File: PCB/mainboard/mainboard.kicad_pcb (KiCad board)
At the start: 2 copper layers, 100 x 68 mm, 1 part, among them IC1 STM32H743ZIT6

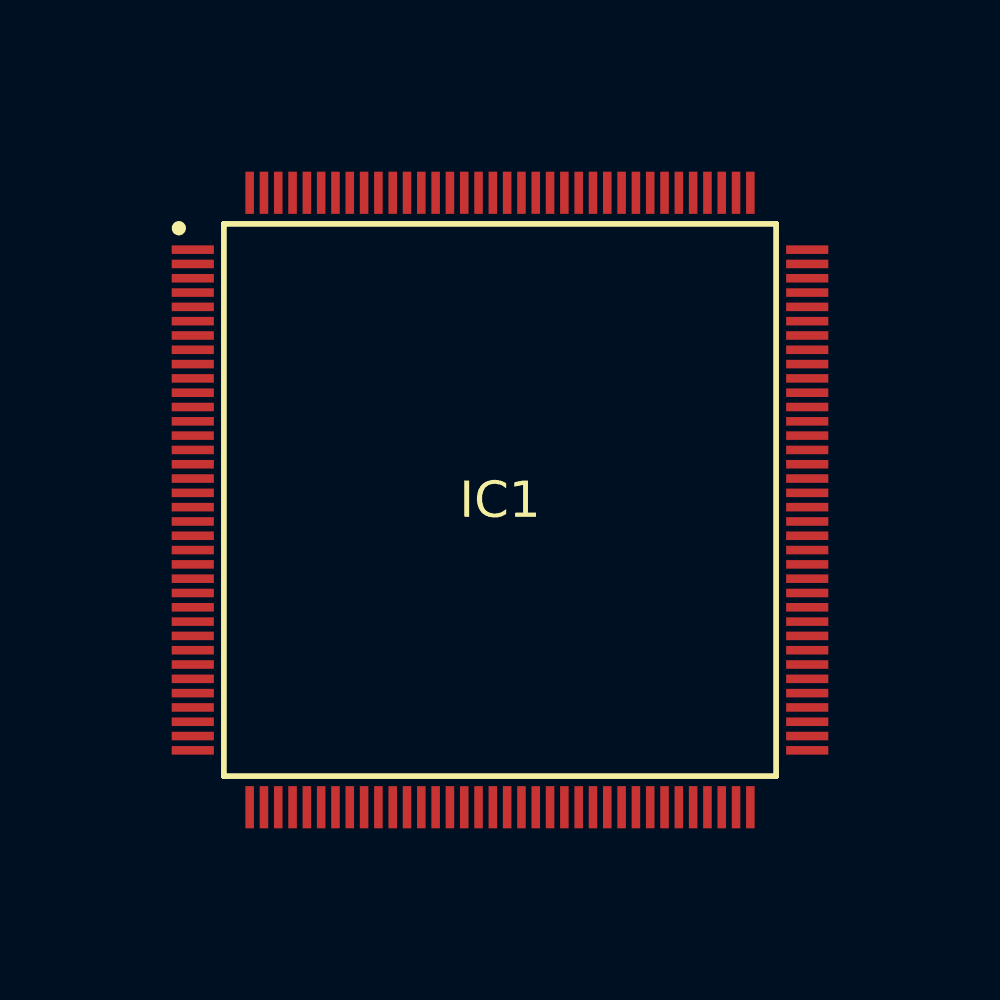
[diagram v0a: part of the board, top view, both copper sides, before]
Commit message: upgrades to STM32 Board
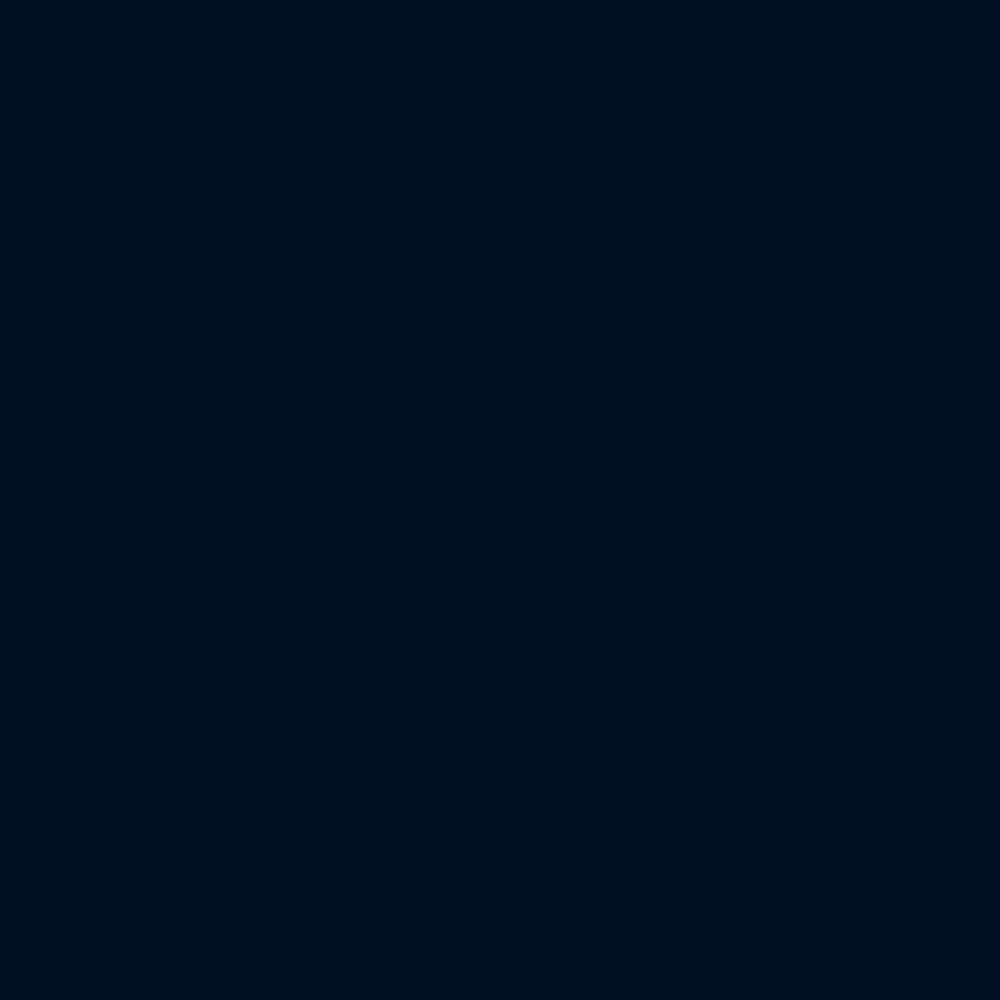
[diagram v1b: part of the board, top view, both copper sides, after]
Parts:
- removed IC1: STM32H743ZIT6, lib:QFP50P2200X2200X160-144N

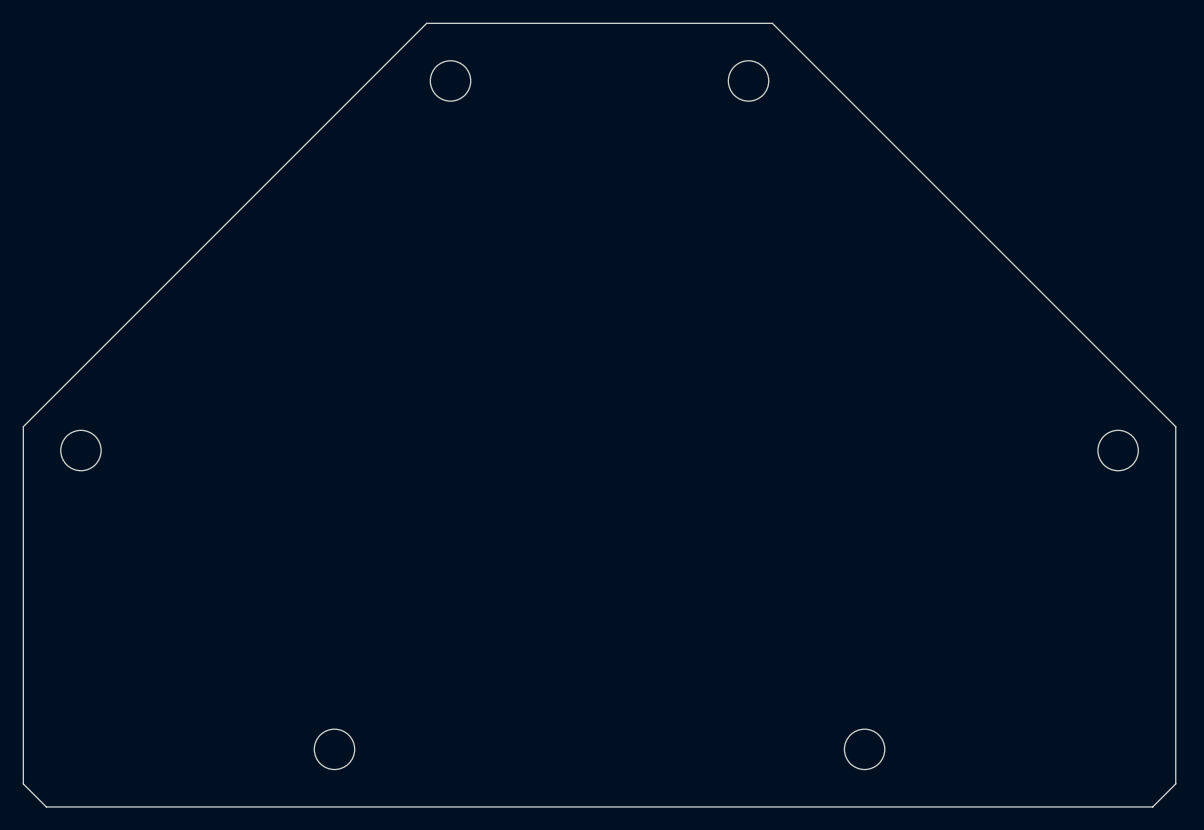
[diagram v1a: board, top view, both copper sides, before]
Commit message: Made the Mainboard BCP Part Layout
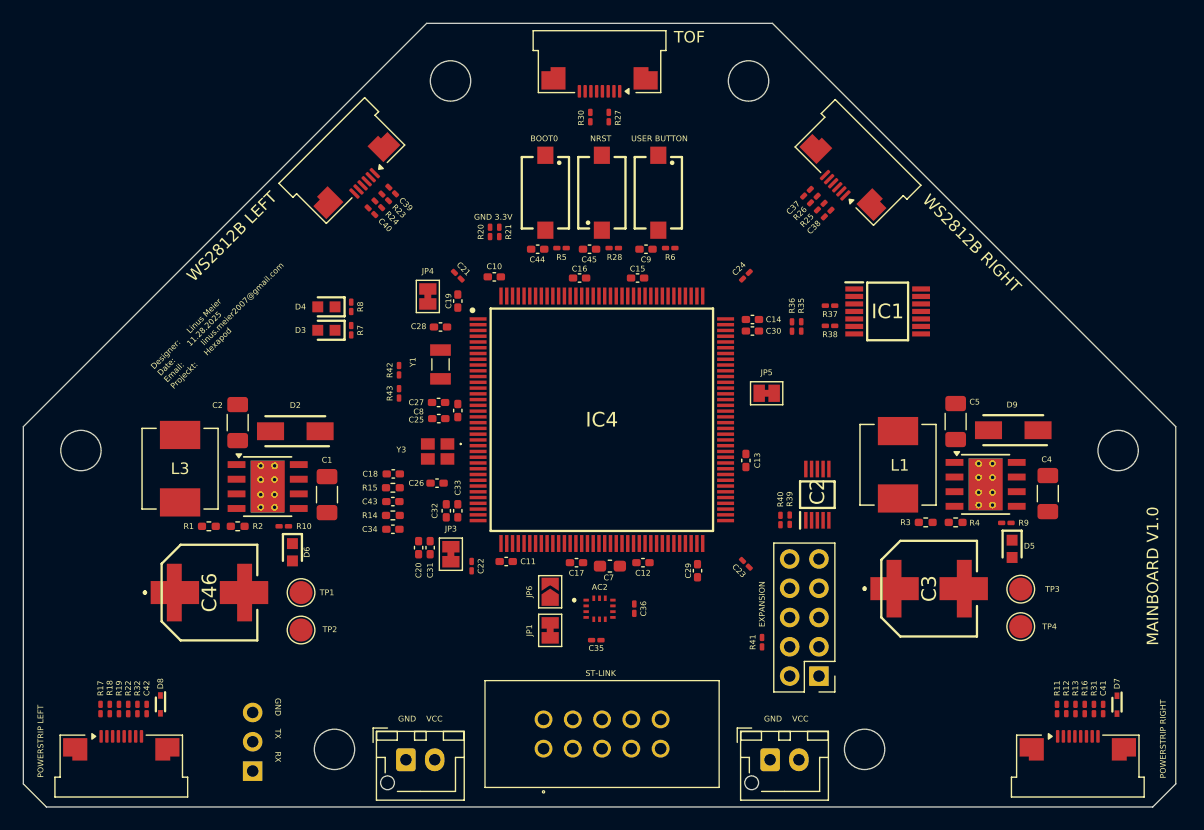
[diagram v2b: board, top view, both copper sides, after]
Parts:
- added AC2: LSM6DSOTR, lib:LSM6DS3USTR, F.Cu at (149.5, 119.3)
- added BOOT0: 434121025816, lib:434121025816, F.Cu at (144.8, 83.2)
- added C1: 10u, Capacitor_SMD:C_1206_3216Metric_Pad1.33x1.80mm_HandSolder, F.Cu at (125.8, 109.4)
- added C10: 100nF, Capacitor_SMD:C_0402_1005Metric_Pad0.74x0.62mm_HandSolder, F.Cu at (140.4, 90.5)
- added C11: 100nF, Capacitor_SMD:C_0402_1005Metric_Pad0.74x0.62mm_HandSolder, F.Cu at (141.4, 115.2)
- added C12: 100nF, Capacitor_SMD:C_0402_1005Metric_Pad0.74x0.62mm_HandSolder, F.Cu at (153.3, 115.3)
- added C13: 100nF, Capacitor_SMD:C_0402_1005Metric_Pad0.74x0.62mm_HandSolder, F.Cu at (162.2, 106.4)
- added C14: 100nF, Capacitor_SMD:C_0402_1005Metric_Pad0.74x0.62mm_HandSolder, F.Cu at (162.8, 94.2)
- added C15: 100nF, Capacitor_SMD:C_0402_1005Metric_Pad0.74x0.62mm_HandSolder, F.Cu at (152.8, 90.6)
- added C16: 100nF, Capacitor_SMD:C_0402_1005Metric_Pad0.74x0.62mm_HandSolder, F.Cu at (147.8, 90.6)
- added C17: 100nF, Capacitor_SMD:C_0402_1005Metric_Pad0.74x0.62mm_HandSolder, F.Cu at (147.5, 115.3)
- added C18: 100nF, Capacitor_SMD:C_0402_1005Metric_Pad0.74x0.62mm_HandSolder, F.Cu at (131.6, 107.6)
- added C19: 1uF, Capacitor_SMD:C_0402_1005Metric_Pad0.74x0.62mm_HandSolder, F.Cu at (137.2, 92.6)
- added C2: 10n, Capacitor_SMD:C_1206_3216Metric_Pad1.33x1.80mm_HandSolder, F.Cu at (118.1, 103.1)
- added C20: 1uF, Capacitor_SMD:C_0402_1005Metric_Pad0.74x0.62mm_HandSolder, F.Cu at (133.8, 114.0)
- added C21: 1u, Capacitor_SMD:C_0201_0603Metric_Pad0.64x0.40mm_HandSolder, F.Cu at (137.2, 90.4)
- added C22: 1u, Capacitor_SMD:C_0201_0603Metric_Pad0.64x0.40mm_HandSolder, F.Cu at (138.4, 115.6)
- added C23: 1u, Capacitor_SMD:C_0201_0603Metric_Pad0.64x0.40mm_HandSolder, F.Cu at (162.2, 115.4)
- added C24: 1u, Capacitor_SMD:C_0201_0603Metric_Pad0.64x0.40mm_HandSolder, F.Cu at (162.2, 90.4)
- added C25: 10pF, Capacitor_SMD:C_0402_1005Metric_Pad0.74x0.62mm_HandSolder, F.Cu at (135.6, 102.8)
- added C26: 10pF, Capacitor_SMD:C_0402_1005Metric_Pad0.74x0.62mm_HandSolder, F.Cu at (135.4, 108.4)
- added C27: 8pF, Capacitor_SMD:C_0402_1005Metric_Pad0.74x0.62mm_HandSolder, F.Cu at (135.5, 101.4)
- added C28: 8pF, Capacitor_SMD:C_0402_1005Metric_Pad0.74x0.62mm_HandSolder, F.Cu at (135.7, 94.8)
- added C29: 2.2u, Capacitor_SMD:C_0402_1005Metric_Pad0.74x0.62mm_HandSolder, F.Cu at (158.0, 116.0)
- added C3: EEE-FP0J331AV 220u, lib:EEEFP0J331AV, F.Cu at (178.1, 117.6)
- added C30: 2.2u, Capacitor_SMD:C_0402_1005Metric_Pad0.74x0.62mm_HandSolder, F.Cu at (162.8, 95.2)
- added C31: 100nF, Capacitor_SMD:C_0402_1005Metric_Pad0.74x0.62mm_HandSolder, F.Cu at (134.8, 114.0)
- added C32: 1uF, Capacitor_SMD:C_0402_1005Metric_Pad0.74x0.62mm_HandSolder, F.Cu at (136.2, 110.8)
- added C33: 100nF, Capacitor_SMD:C_0402_1005Metric_Pad0.74x0.62mm_HandSolder, F.Cu at (137.2, 110.8)
- added C34: 100nF, Capacitor_SMD:C_0402_1005Metric_Pad0.74x0.62mm_HandSolder, F.Cu at (131.6, 112.4)
- added C35: 100n, Capacitor_SMD:C_0201_0603Metric_Pad0.64x0.40mm_HandSolder, F.Cu at (149.2, 122.0)
- added C36: 100n, Capacitor_SMD:C_0201_0603Metric_Pad0.64x0.40mm_HandSolder, F.Cu at (152.5, 119.3)
- added C37: 1u, Capacitor_SMD:C_0201_0603Metric_Pad0.64x0.40mm_HandSolder, F.Cu at (167.5, 83.2)
- added C38: 1u, Capacitor_SMD:C_0201_0603Metric_Pad0.64x0.40mm_HandSolder, F.Cu at (169.3, 85.0)
- added C39: 1u, Capacitor_SMD:C_0201_0603Metric_Pad0.64x0.40mm_HandSolder, F.Cu at (131.5, 83.0)
- added C4: 10u, Capacitor_SMD:C_1206_3216Metric_Pad1.33x1.80mm_HandSolder, F.Cu at (188.4, 109.3)
- added C40: 1u, Capacitor_SMD:C_0201_0603Metric_Pad0.64x0.40mm_HandSolder, F.Cu at (129.7, 84.8)
- added C41: 100n, Capacitor_SMD:C_0201_0603Metric_Pad0.64x0.40mm_HandSolder, F.Cu at (193.2, 128.0)
- added C42: 100n, Capacitor_SMD:C_0201_0603Metric_Pad0.64x0.40mm_HandSolder, F.Cu at (110.2, 128.0)
- added C43: 100nF, Capacitor_SMD:C_0402_1005Metric_Pad0.74x0.62mm_HandSolder, F.Cu at (131.6, 110.0)
- added C44: 100n, Capacitor_SMD:C_0402_1005Metric_Pad0.74x0.62mm_HandSolder, F.Cu at (144.1, 88.1)
- added C45: 100n, Capacitor_SMD:C_0402_1005Metric_Pad0.74x0.62mm_HandSolder, F.Cu at (148.6, 88.1)
- added C46: EEE-FP0J331AV 220u, lib:EEEFP0J331AV, F.Cu at (115.7, 117.9)
- added C5: 10n, Capacitor_SMD:C_1206_3216Metric_Pad1.33x1.80mm_HandSolder, F.Cu at (180.4, 103.1)
- added C7: 4.7uF, Capacitor_SMD:C_0603_1608Metric_Pad1.08x0.95mm_HandSolder, F.Cu at (150.4, 115.6)
- added C8: 100nF, Capacitor_SMD:C_0402_1005Metric_Pad0.74x0.62mm_HandSolder, F.Cu at (137.2, 102.1)
- added C9: 100n, Capacitor_SMD:C_0402_1005Metric_Pad0.74x0.62mm_HandSolder, F.Cu at (153.5, 88.1)
- added D2: B340A-13-F, lib:DIOM5226X240N, F.Cu at (123.1, 103.9)
- added D3: LED_Red, lib:LEDC1608X70N, F.Cu at (125.8, 95.1)
- added D4: LED_Geen, lib:LEDC1608X70N, F.Cu at (125.8, 93.1)
- added D5: LED_Geen, lib:LEDC1608X70N, F.Cu at (185.3, 114.1)
- added D6: LED_Geen, lib:LEDC1608X70N, F.Cu at (122.8, 114.4)
- added D7: BZT585B3V3T-7, lib:SODFL1608X65N, F.Cu at (194.4, 127.6)
- added D8: BZT585B3V3T-7, lib:SODFL1608X65N, F.Cu at (111.4, 127.6)
- added D9: B340A-13-F, lib:DIOM5226X240N, F.Cu at (185.4, 103.8)
- added EXPANSION: Conn_02x05_Counter_Clockwise, Connector_PinHeader_2.54mm:PinHeader_2x05_P2.54mm_Vertical, F.Cu at (168.5, 125.1)
- added GND    VCC: Right Strip Power, Connector_JST:JST_XH_B2B-XH-AM_1x02_P2.50mm_Vertical, F.Cu at (164.3, 132.4)
- added GND    VCC: Left Strip Power, Connector_JST:JST_XH_B2B-XH-AM_1x02_P2.50mm_Vertical, F.Cu at (132.7, 132.4)
- added IC1: 74HCT125T14-13, lib:SOP65P640X120-14N, F.Cu at (174.5, 93.5)
- added IC2: SP4065-08ATG, lib:SOP50P488X110-10N, F.Cu at (168.4, 109.4)
- added IC4: STM32H743ZIT6, lib:QFP50P2200X2200X160-144N, F.Cu at (149.7, 102.9)
- added J10: Uart Connector to pi5, Connector_PinSocket_2.54mm:PinSocket_1x03_P2.54mm_Vertical, B.Cu at (119.4, 133.4)
- added JP1: SolderJumper_2_Bridged, Jumper:SolderJumper-2_P1.3mm_Bridged_Pad1.0x1.5mm, F.Cu at (145.2, 121.2)
- added JP3: SolderJumper_2_Bridged, Jumper:SolderJumper-2_P1.3mm_Bridged_Pad1.0x1.5mm, F.Cu at (136.6, 114.6)
- added JP4: SolderJumper_2_Bridged, Jumper:SolderJumper-2_P1.3mm_Bridged_Pad1.0x1.5mm, F.Cu at (134.6, 92.2)
- added JP5: SolderJumper_2_Bridged, Jumper:SolderJumper-2_P1.3mm_Bridged_Pad1.0x1.5mm, F.Cu at (164.0, 100.6)
- added JP6: SolderJumper_2_Open, Jumper:SolderJumper-2_P1.3mm_Open_TrianglePad1.0x1.5mm, F.Cu at (145.2, 117.8)
- added L1: MGAH06033R3M-10, lib:IND_MGAH06033R3M-10, F.Cu at (175.4, 106.8)
- added L3: MGAH06033R3M-10, lib:IND_MGAH06033R3M-10, F.Cu at (113.1, 107.1)
- added NRST: 434121025816, lib:434121025816, F.Cu at (149.7, 83.2)
- added POWERSTRIP LEFT: Left Strip, Connector_FFC-FPC:Amphenol_F32Q-1A7x1-11008_1x08-1MP_P0.5mm_Horizontal, F.Cu at (108.0, 133.3)
- added POWERSTRIP RIGHT: Right Strip, Connector_FFC-FPC:Amphenol_F32Q-1A7x1-11008_1x08-1MP_P0.5mm_Horizontal, F.Cu at (191.0, 133.3)
- added R1: 51k, Resistor_SMD:R_0402_1005Metric_Pad0.72x0.64mm_HandSolder, F.Cu at (115.6, 112.1)
- added R10: 270R, Resistor_SMD:R_0201_0603Metric_Pad0.64x0.40mm_HandSolder, F.Cu at (122.1, 112.1)
- added R11: 47R, Resistor_SMD:R_0201_0603Metric_Pad0.64x0.40mm_HandSolder, F.Cu at (189.2, 128.0)
- added R12: 47R, Resistor_SMD:R_0201_0603Metric_Pad0.64x0.40mm_HandSolder, F.Cu at (190.0, 128.0)
- added R13: 47R, Resistor_SMD:R_0201_0603Metric_Pad0.64x0.40mm_HandSolder, F.Cu at (190.8, 128.0)
- added R14: 0R, Resistor_SMD:R_0402_1005Metric_Pad0.72x0.64mm_HandSolder, F.Cu at (131.6, 111.2)
- added R15: 0R, Resistor_SMD:R_0402_1005Metric_Pad0.72x0.64mm_HandSolder, F.Cu at (131.6, 108.8)
- added R16: 47R, Resistor_SMD:R_0201_0603Metric_Pad0.64x0.40mm_HandSolder, F.Cu at (191.6, 128.0)
- added R17: 47R, Resistor_SMD:R_0201_0603Metric_Pad0.64x0.40mm_HandSolder, F.Cu at (106.2, 128.0)
- added R18: 47R, Resistor_SMD:R_0201_0603Metric_Pad0.64x0.40mm_HandSolder, F.Cu at (107.0, 128.0)
- added R19: 47R, Resistor_SMD:R_0201_0603Metric_Pad0.64x0.40mm_HandSolder, F.Cu at (107.8, 128.0)
- added R2: 10k, Resistor_SMD:R_0402_1005Metric_Pad0.72x0.64mm_HandSolder, F.Cu at (118.1, 112.1)
- added R20: 10k, Resistor_SMD:R_0201_0603Metric_Pad0.64x0.40mm_HandSolder, F.Cu at (140.0, 86.6)
- added R21: 10k, Resistor_SMD:R_0201_0603Metric_Pad0.64x0.40mm_HandSolder, F.Cu at (140.8, 86.6)
- added R22: 47R, Resistor_SMD:R_0201_0603Metric_Pad0.64x0.40mm_HandSolder, F.Cu at (108.6, 128.0)
- added R23: 47R, Resistor_SMD:R_0201_0603Metric_Pad0.64x0.40mm_HandSolder, F.Cu at (130.9, 83.6)
- added R24: 47R, Resistor_SMD:R_0201_0603Metric_Pad0.64x0.40mm_HandSolder, F.Cu at (130.3, 84.2)
- added R25: 47R, Resistor_SMD:R_0201_0603Metric_Pad0.64x0.40mm_HandSolder, F.Cu at (168.7, 84.4)
- added R26: 47R, Resistor_SMD:R_0201_0603Metric_Pad0.64x0.40mm_HandSolder, F.Cu at (168.1, 83.8)
- added R27: 47R, Resistor_SMD:R_0201_0603Metric_Pad0.64x0.40mm_HandSolder, F.Cu at (150.3, 76.6)
- added R28: 10k, Resistor_SMD:R_0201_0603Metric_Pad0.64x0.40mm_HandSolder, F.Cu at (150.7, 88.0)
- added R3: 31.6k, Resistor_SMD:R_0402_1005Metric_Pad0.72x0.64mm_HandSolder, F.Cu at (177.8, 111.8)
- added R30: 47R, Resistor_SMD:R_0201_0603Metric_Pad0.64x0.40mm_HandSolder, F.Cu at (148.7, 76.6)
- added R31: 10R, Resistor_SMD:R_0201_0603Metric_Pad0.64x0.40mm_HandSolder, F.Cu at (192.4, 128.0)
- added R32: 10R, Resistor_SMD:R_0201_0603Metric_Pad0.64x0.40mm_HandSolder, F.Cu at (109.4, 128.0)
- added R35: 4.7k, Resistor_SMD:R_0201_0603Metric_Pad0.64x0.40mm_HandSolder, F.Cu at (167.0, 94.8)
- added R36: 4.7k, Resistor_SMD:R_0201_0603Metric_Pad0.64x0.40mm_HandSolder, F.Cu at (166.2, 94.8)
- added R37: 330R, Resistor_SMD:R_0201_0603Metric_Pad0.64x0.40mm_HandSolder, F.Cu at (169.5, 93.0)
- added R38: 330R, Resistor_SMD:R_0201_0603Metric_Pad0.64x0.40mm_HandSolder, F.Cu at (169.5, 94.8)
- added R39: 47R, Resistor_SMD:R_0201_0603Metric_Pad0.64x0.40mm_HandSolder, F.Cu at (166.0, 111.6)
- added R4: 10k, Resistor_SMD:R_0402_1005Metric_Pad0.72x0.64mm_HandSolder, F.Cu at (180.4, 111.8)
- added R40: 47R, Resistor_SMD:R_0201_0603Metric_Pad0.64x0.40mm_HandSolder, F.Cu at (165.2, 111.6)
- added R41: 47R, Resistor_SMD:R_0201_0603Metric_Pad0.64x0.40mm_HandSolder, F.Cu at (163.6, 122.2)
- added R42: 100k, Resistor_SMD:R_0201_0603Metric_Pad0.64x0.40mm_HandSolder, F.Cu at (132.1, 98.6)
- added R43: 10k, Resistor_SMD:R_0201_0603Metric_Pad0.64x0.40mm_HandSolder, F.Cu at (132.1, 100.6)
- added R5: 10k, Resistor_SMD:R_0201_0603Metric_Pad0.64x0.40mm_HandSolder, F.Cu at (146.2, 88.0)
- added R6: 10k, Resistor_SMD:R_0201_0603Metric_Pad0.64x0.40mm_HandSolder, F.Cu at (155.6, 88.0)
- added R7: 100R, Resistor_SMD:R_0201_0603Metric_Pad0.64x0.40mm_HandSolder, F.Cu at (128.0, 95.1)
- added R8: 100R, Resistor_SMD:R_0201_0603Metric_Pad0.64x0.40mm_HandSolder, F.Cu at (128.0, 93.1)
- added R9: 100R, Resistor_SMD:R_0201_0603Metric_Pad0.64x0.40mm_HandSolder, F.Cu at (184.8, 111.8)
- added ST-LINK: TST-105-01-L-D, lib:TST-105-XX-Y-D, F.Cu at (144.6, 131.4)
- added TOF: Time Of Flight, Connector_FFC-FPC:Amphenol_F32Q-1A7x1-11008_1x08-1MP_P0.5mm_Horizontal, F.Cu at (149.5, 71.5)
- added TP1: TestPoint, TestPoint:TestPoint_Pad_D2.0mm, F.Cu at (123.6, 117.9)
- added TP2: TestPoint, TestPoint:TestPoint_Pad_D2.0mm, F.Cu at (123.6, 121.1)
- added TP3: TestPoint, TestPoint:TestPoint_Pad_D2.0mm, F.Cu at (186.1, 117.6)
- added TP4: TestPoint, TestPoint:TestPoint_Pad_D2.0mm, F.Cu at (186.1, 120.8)
- added U1: TPS5430DDA, Package_SO:TI_SO-PowerPAD-8_ThermalVias, F.Cu at (120.7, 108.7)
- added U2: TPS5430DDA, Package_SO:TI_SO-PowerPAD-8_ThermalVias, F.Cu at (183.0, 108.5)
- added USER BUTTON: 434121025816, lib:434121025816, F.Cu at (154.6, 83.2)
- added WS2812B LEFT: LED Strip left, Connector_FFC-FPC:Amphenol_F32Q-1A7x1-11006_1x06-1MP_P0.5mm_Horizontal, F.Cu at (127.1, 80.3)
- added WS2812B RIGHT: LED Strip right, Connector_FFC-FPC:Amphenol_F32Q-1A7x1-11006_1x06-1MP_P0.5mm_Horizontal, F.Cu at (172.0, 80.5)
- added Y1: CM7V-T1A-32.768KHZ-7PF-20PPM-TA-QC, lib:CM7V32768TBQA020, F.Cu at (135.7, 98.1)
- added Y3: ECS-250-8-36CKM-TR3, lib:ECS250836CKMTR3, F.Cu at (135.4, 105.7)
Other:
- board text added: "Designer: Linus Meier Date: 11.28.2025 Email: linus.meier2007@gmail.com Projeckt: Hexapod"
- board text added: "GND 3.3V"
- board text added: "GND TX RX"
- board text added: "MAINBOARD V1.0"

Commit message: Stop tracking renders folder & final Powerstrip and Mainboard PCB
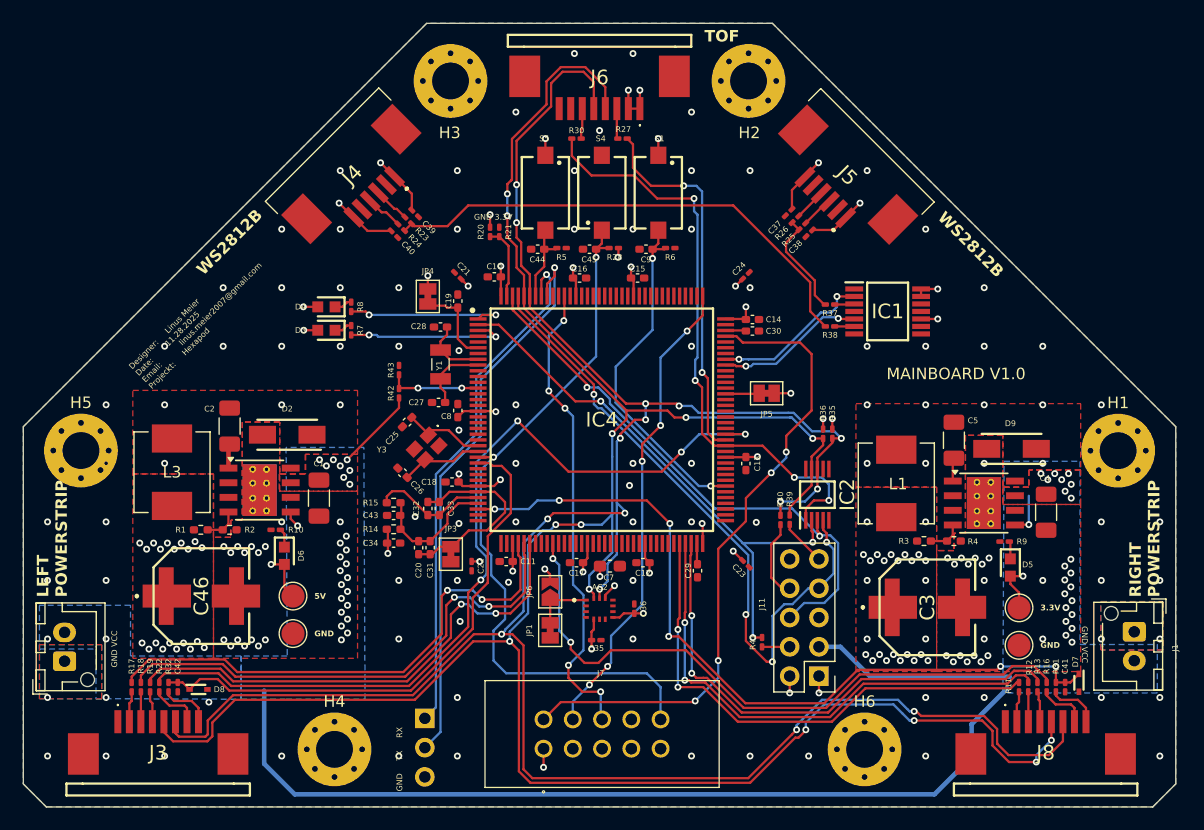
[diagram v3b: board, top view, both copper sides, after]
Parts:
- added H1: MountingHole_Pad, MountingHole:MountingHole_3.2mm_M3_Pad_Via, F.Cu at (194.5, 105.6)
- added H2: MountingHole_Pad, MountingHole:MountingHole_3.2mm_M3_Pad_Via, F.Cu at (162.4, 73.5)
- added H3: MountingHole_Pad, MountingHole:MountingHole_3.2mm_M3_Pad_Via, F.Cu at (136.6, 73.5)
- added H4: MountingHole_Pad, MountingHole:MountingHole_3.2mm_M3_Pad_Via, F.Cu at (126.5, 131.5)
- added H5: MountingHole_Pad, MountingHole:MountingHole_3.2mm_M3_Pad_Via, F.Cu at (104.5, 105.6)
- added H6: MountingHole_Pad, MountingHole:MountingHole_3.2mm_M3_Pad_Via, F.Cu at (172.5, 131.5)
- J1, J2: renamed from GND    VCC
- J3: renamed from POWERSTRIP LEFT; footprint Connector_FFC-FPC:Amphenol_F32Q-1A7x1-11008_1x08-1MP_P0.5mm_Horizontal -> lib:17352658
- J4: renamed from WS2812B LEFT; footprint Connector_FFC-FPC:Amphenol_F32Q-1A7x1-11006_1x06-1MP_P0.5mm_Horizontal -> lib:849526
- J5: renamed from WS2812B RIGHT; footprint Connector_FFC-FPC:Amphenol_F32Q-1A7x1-11006_1x06-1MP_P0.5mm_Horizontal -> lib:849526
- J6: renamed from TOF; footprint Connector_FFC-FPC:Amphenol_F32Q-1A7x1-11008_1x08-1MP_P0.5mm_Horizontal -> lib:17352658
- J8: renamed from POWERSTRIP RIGHT; footprint Connector_FFC-FPC:Amphenol_F32Q-1A7x1-11008_1x08-1MP_P0.5mm_Horizontal -> lib:17352658
- S1: renamed from USER BUTTON
- moved J1 33.5 mm to (195.9, 121.3), turned to -90 degrees
- moved J2 30.8 mm to (103.1, 123.8), turned to 90 degrees
- moved J10 15.6 mm to (134.3, 128.8), turned to 180 degrees
- moved R35 9.69 mm to (169.7, 104.1)
- moved R36 9.69 mm to (168.9, 104.1)
- moved C18 5.15 mm to (136.7, 108.3)
- moved D7 3.81 mm to (191.1, 125.7)
- moved R12 3.81 mm to (186.7, 126.1)
- moved R13 3.81 mm to (187.5, 126.1)
- moved R31 3.81 mm to (189.1, 126.1)
- moved C41 3.81 mm to (189.9, 126.1)
- moved R11 3.81 mm to (185.9, 126.1)
- moved R16 3.81 mm to (188.3, 126.1)
- moved D8 3.55 mm to (114.7, 126.3), turned to 0 degrees
- moved J3 3.35 mm to (111.2, 132.3)
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- renumbered EXPANSION to J11, ST-LINK to J7, NRST to S4, BOOT0 to S5
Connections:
- net Net-(D2-K) renamed PH 5
- net Net-(D9-K) renamed PH 3.3
- IC4 pad 37: right_A2 -> unconnected-(IC4-PA3-Pad37)
- IC4 pad 40: right_A1 -> left_A2
- IC4 pad 41: right_A0 -> left_A1
- IC4 pad 42: unconnected-(IC4-PA6-Pad42) -> left_A0
- IC4 pad 68: unconnected-(IC4-PE15-Pad68) -> right_A2
- IC4 pad 69: unconnected-(IC4-PB10-Pad69) -> right_A1
- IC4 pad 70: unconnected-(IC4-PB11-Pad70) -> right_A0
- IC4 pad 73: left_A0 -> unconnected-(IC4-PB12-Pad73)
- IC4 pad 74: left_A1 -> unconnected-(IC4-PB13-Pad74)
- IC4 pad 75: left_A2 -> unconnected-(IC4-PB14-Pad75)
- J11 pad 2: +5V -> GND
- J11 pad 5: GND -> +5V
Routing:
- net SCL: track 0.00 -> 211.3 mm, vias 0 -> 15
- net SDA: track 0.00 -> 206.2 mm, vias 0 -> 13
- net VCC: track 0.00 -> 107.5 mm, vias 0 -> 18
- net left_¬EN: track 0.00 -> 74.9 mm, vias 0 -> 4
- net +3V3: track 0.00 -> 69.6 mm, vias 0 -> 57
- net right_ADC INPUT: track 0.00 -> 68.6 mm, vias 0 -> 6
- net NRST: track 0.00 -> 63.8 mm, vias 0 -> 2
- net GPIO Expansion 1: track 0.00 -> 57.4 mm, vias 0 -> 4
- net right_¬EN: track 0.00 -> 56.4 mm, vias 0 -> 2
- net SWDIO: track 0.00 -> 56.2 mm, vias 0 -> 4
- net XSHUT: track 0.00 -> 52.0 mm, vias 0 -> 4
- net TX: track 0.00 -> 49.0 mm, vias 0 -> 1
- net GPIO Expansion 2: track 0.00 -> 49.0 mm, vias 0 -> 2
- net GPIO Expansion 3: track 0.00 -> 48.3 mm, vias 0 -> 3
- net left_ADC INPUT: track 0.00 -> 47.6 mm
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- added copper zone on F.Cu, net +3V3
- added copper zone on In2.Cu, net +3V3
- added copper zone on B.Cu, net +5V
- added copper zone on F.Cu, net +5V
- added copper zone on B.Cu, net GND
- added copper zone on F.Cu, net GND
- added copper zone on In1.Cu, net GND
- added copper zone on In2.Cu, net GND
- added copper zone on F.Cu, net PH 3.3
- added copper zone on F.Cu, net PH 5
- added copper zone on B.Cu, net VCC
- added copper zone on F.Cu, net VCC
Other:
- outline, holes or cut-outs redrawn
- copper layers 2 -> 4
- board text added: "3.3V"
- board text added: "5V"
- board text added: "GND"
- board text added: "GND VCC"
- board text added: "LEFT POWERSTRIP"
- board text added: "RIGHT POWERSTRIP"
- board text added: "TOF"
- board text added: "WS2812B"
